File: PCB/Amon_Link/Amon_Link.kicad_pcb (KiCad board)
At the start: 4 copper layers, 55 x 40 mm, 103 parts, among them IC1 SPX5205M5-L/TR, J1 USB_C_Receptacle_USB2.0, J2 SMA Edge, J3 Programing port, J4 SMA Edge, SW1 SW_SPST, U1 CH32V003F4P6, U2 CH340G, U3 NRF24L01, U4 RFX2401C, U5 NRF24L01, U6 RFX2401C, Y2 12MHz, Y3 16MHz, Y4 16MHz, Y5 24MHz

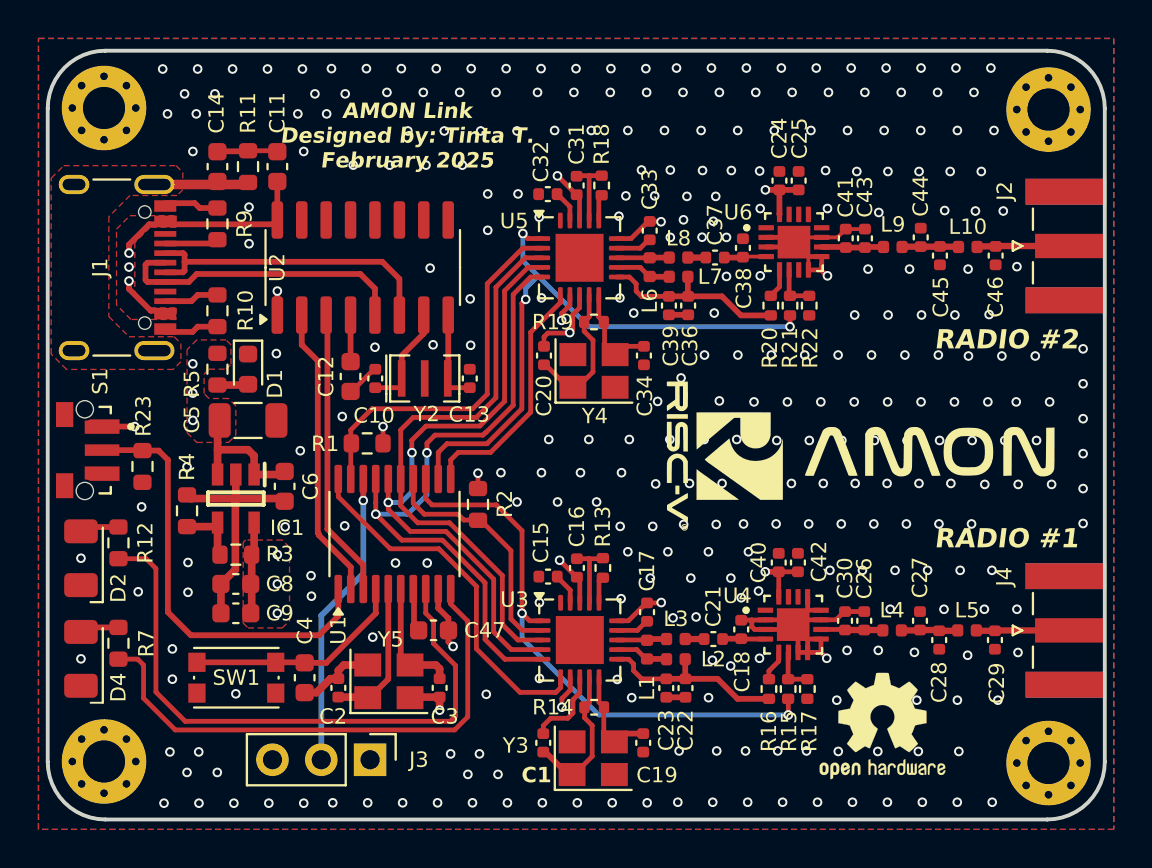
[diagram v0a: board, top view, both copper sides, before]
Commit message: Update
power stability optimization on PCB - added Cs for TX event
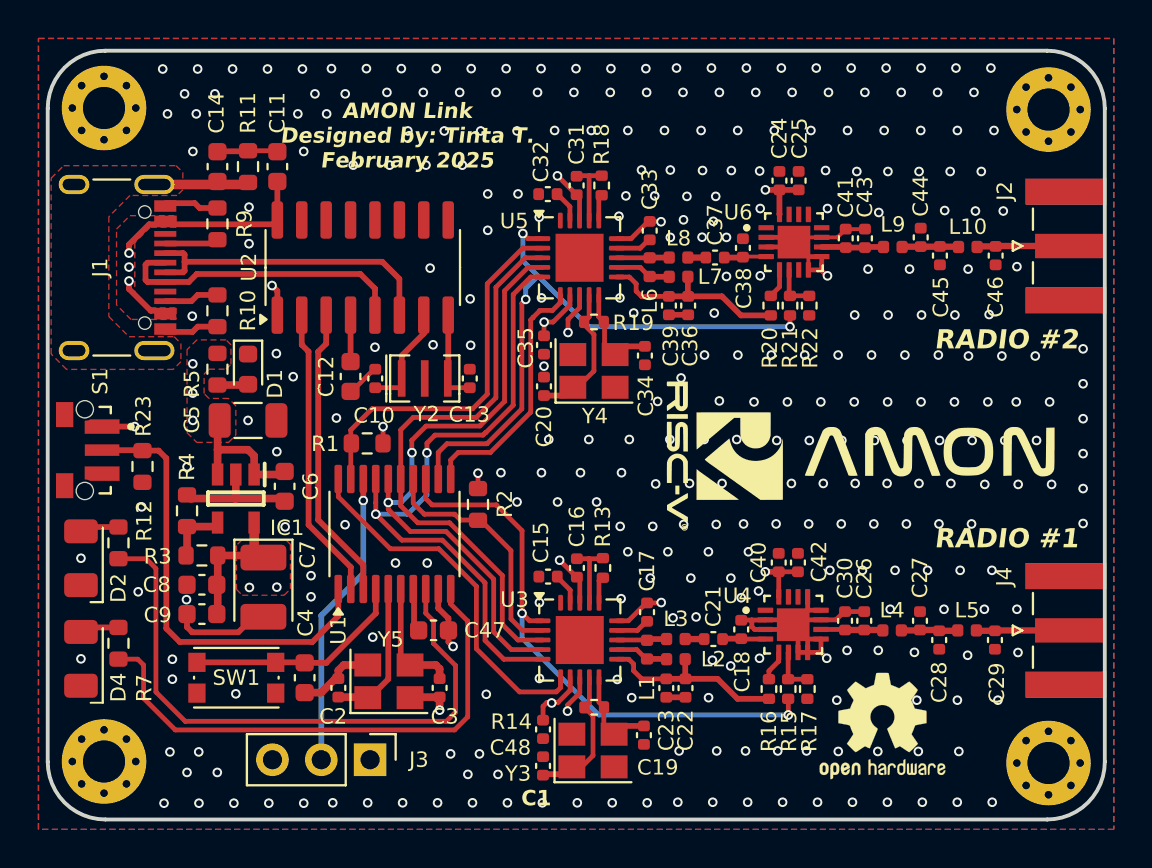
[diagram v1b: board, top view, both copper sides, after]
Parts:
- added C35: 1uF, Capacitor_SMD:C_0402_1005Metric, F.Cu at (152.1, 89.8)
- added C48: 1uF, Capacitor_SMD:C_0402_1005Metric, F.Cu at (152.0, 109.8)
- added C7: tbd, Capacitor_Tantalum_SMD:CP_EIA-3528-12_Kemet-T, F.Cu at (137.4, 102.4)
- C22, C36: value 2.2pF -> 2.2nF
- moved C8 1.77 mm to (134.2, 102.3)
- moved C9 1.77 mm to (134.2, 103.8)
- moved R3 1.77 mm to (134.2, 100.8)
- moved C20 1.60 mm to (152.1, 92.0)
- moved C1 1.20 mm to (152.0, 111.7)
- moved C19 0.40 mm to (157.2, 110.1)
- moved Y3 0.40 mm to (154.6, 110.9)
- moved C34 0.05 mm to (157.3, 90.3)
- turned H1 to 90 degrees
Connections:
- H1 pad 1: (no net) -> GND
- H2 pad 1: (no net) -> GND
- H3 pad 1: (no net) -> GND
- H4 pad 1: (no net) -> GND
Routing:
- net +3.3V: track 31.5 -> 37.3 mm, vias 15 -> 14
- net GND: track 84.4 -> 79.7 mm, vias 311 -> 315
- net /BTN: track 22.7 -> 23.6 mm
- net /IRQ2: track 12.9 -> 13.7 mm
- net Net-(U5-XC1): track 5.13 -> 5.84 mm
- net Net-(U3-XC1): track 5.38 -> 6.04 mm
